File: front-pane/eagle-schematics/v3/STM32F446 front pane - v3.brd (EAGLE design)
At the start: 450 x 300 mm, 707 parts

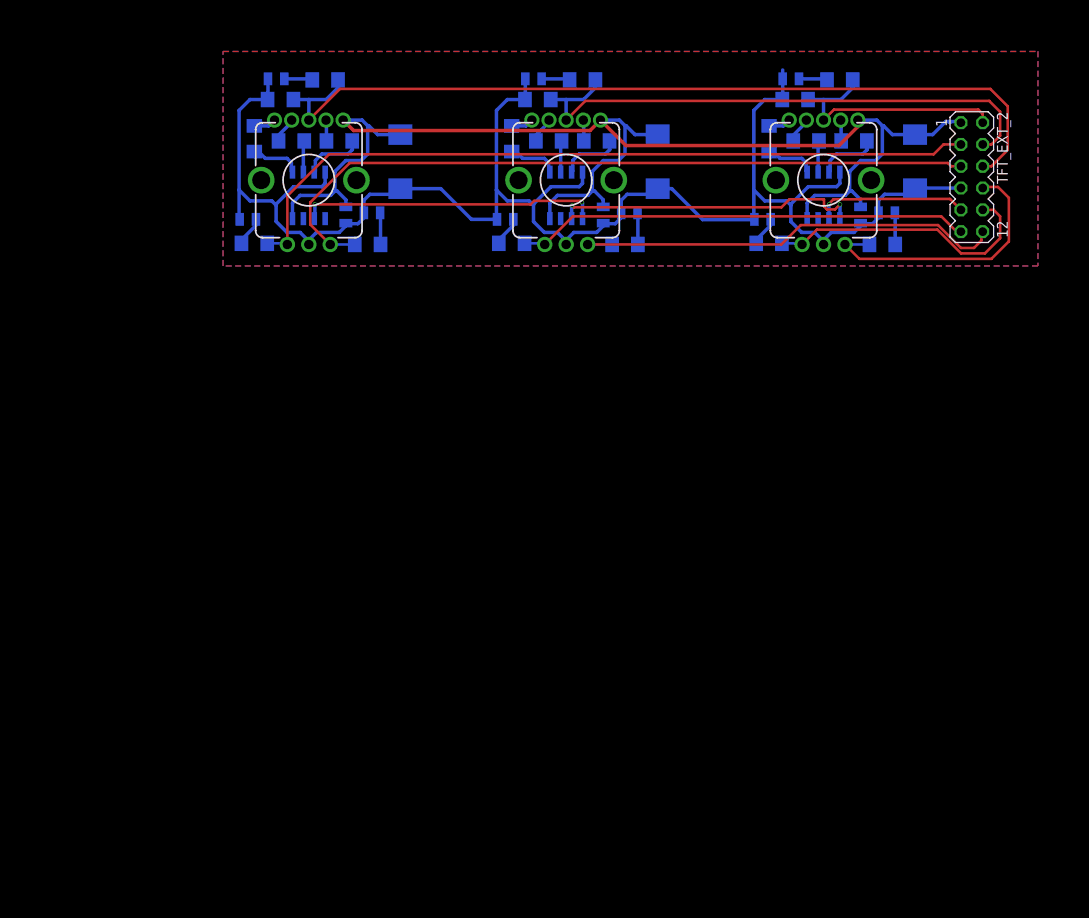
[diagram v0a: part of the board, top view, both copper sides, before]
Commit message: Slight translation of touch screen
This doesn't have any consequence on the electrical design
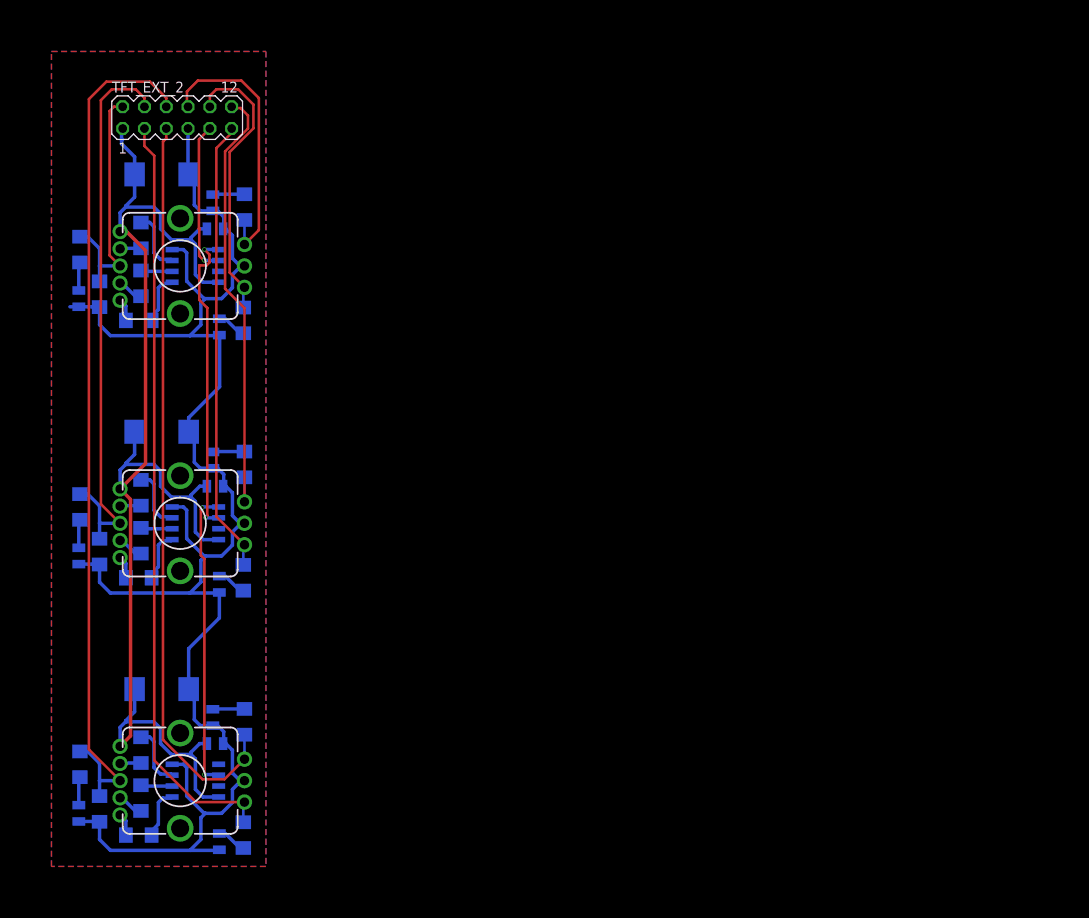
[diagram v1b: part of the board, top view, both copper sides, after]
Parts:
- moved TFT_EXT_2 92.9 mm to (44.6, 267.3), turned to 0 degrees
- moved RB118 90.8 mm to (33.3, 251.9), turned to 270 degrees
- moved CB106 88.7 mm to (33.2, 186.2), turned to 270 degrees
- moved CDEC37 87.8 mm to (42.8, 260.7), turned to 180 degrees
- moved CB118 86.9 mm to (33.2, 246.2), turned to 270 degrees
- moved RPD33 85.3 mm to (35.6, 186.7), turned to 270 degrees
- moved RB106 84.7 mm to (33.3, 191.9), turned to 270 degrees
- moved RPD37 84.2 mm to (35.6, 246.7), turned to 270 degrees
- moved R197 83.9 mm to (40.4, 253.6), turned to 270 degrees
- moved R183 82.3 mm to (40.2, 183.7), turned to 0 degrees
- moved R196 79.3 mm to (40.4, 248.0), turned to 270 degrees
- moved R184 78.6 mm to (40.4, 188.0), turned to 270 degrees
- moved CB117 78.6 mm to (48.8, 257.4), turned to 90 degrees
- moved RB112 76.9 mm to (33.3, 221.9), turned to 270 degrees
- moved CB112 76.8 mm to (33.2, 216.2), turned to 270 degrees
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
